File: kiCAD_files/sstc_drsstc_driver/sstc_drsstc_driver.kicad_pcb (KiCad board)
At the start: 2 copper layers, 90 x 90 mm, 80 parts, among them J1 Conn_01x02, J10 Conn_01x02, J11 Conn_01x03, J12 24V, J13 12V, J14 12V, J15 Conn_01x05, J16 Conn_01x05, J2 GDT, J3 Int_esp, J4 24V, J5 DRSSTC, J6 Conn_01x02, J7 SSTC, J8 DRSSTC, J9 SSTC_DUMMY, Q1 2N3904, U1 UCC27321P, U2 74HC14, U3 UCC27322P, U4 4N35, U5 ESP32-DEVKIT-V1, U7 74HC74, U8 LM7812_TO220, U9 LM7805_TO220

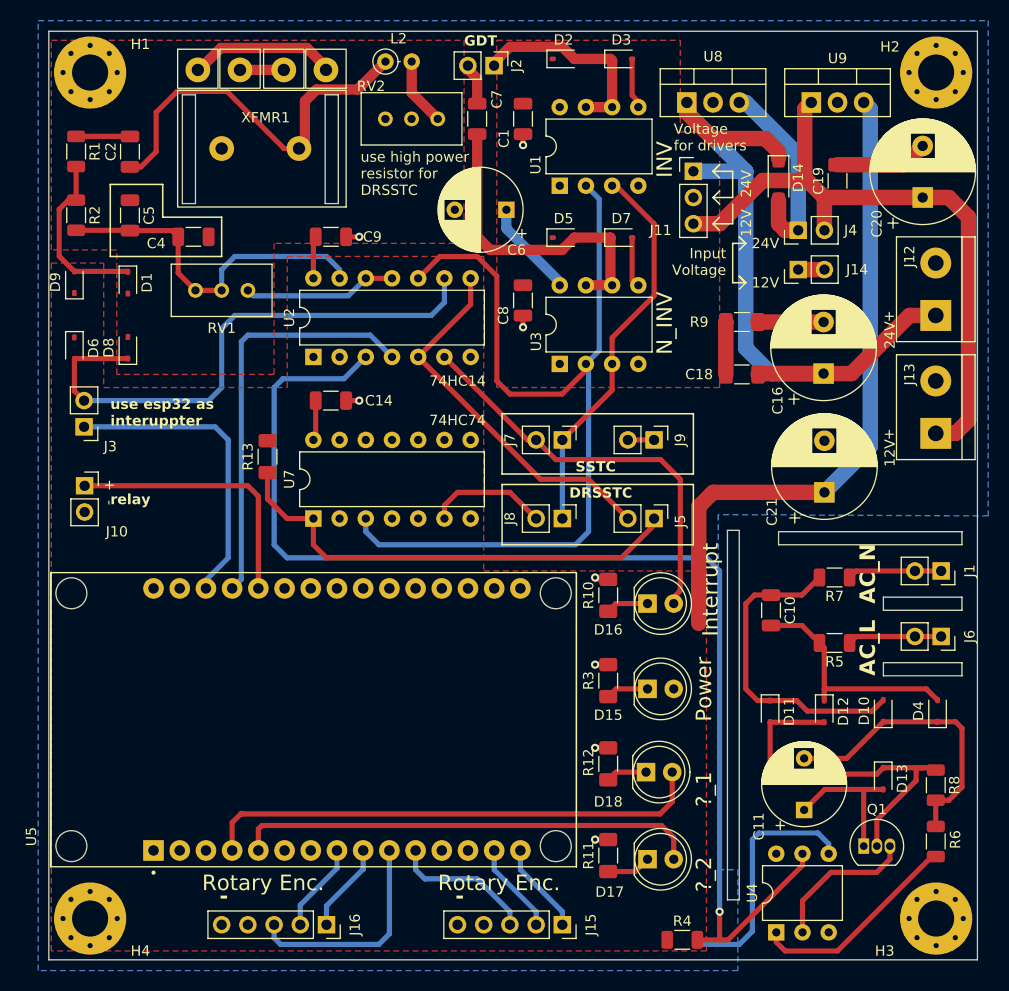
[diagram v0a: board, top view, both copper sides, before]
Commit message: Add files via upload
Rotary encoders are now connected to 3.3V instead of 5V
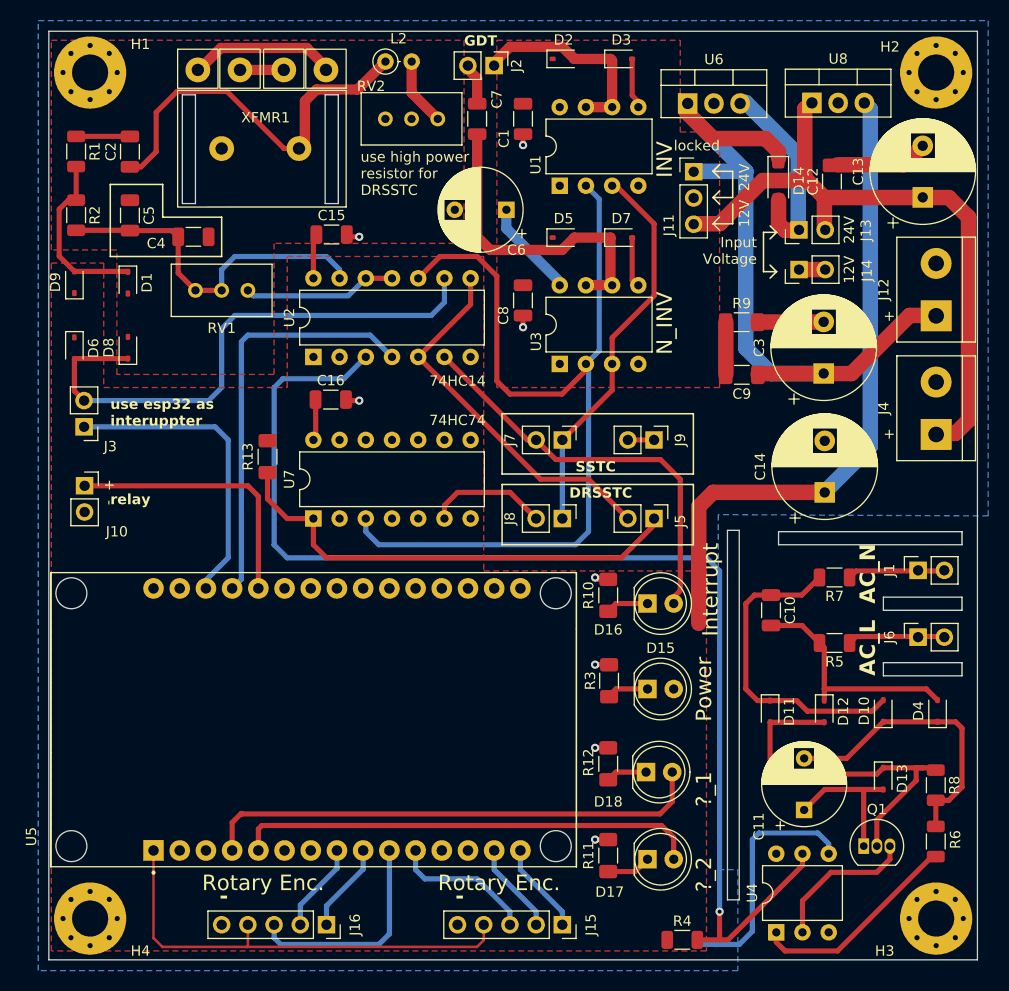
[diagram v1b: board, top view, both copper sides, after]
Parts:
- removed C18: 4.7u, Capacitor_SMD:C_1206_3216Metric_Pad1.33x1.80mm_HandSolder
- removed C19: 100n, Capacitor_SMD:C_1206_3216Metric_Pad1.33x1.80mm_HandSolder
- removed C20, C21: 330u, Capacitor_THT:CP_Radial_D10.0mm_P5.00mm
- removed U9: LM7805_TO220, Package_TO_SOT_THT:TO-220-3_Vertical
- added C12: 100n, Capacitor_SMD:C_1206_3216Metric_Pad1.33x1.80mm_HandSolder, F.Cu at (90.9, 29.6)
- added C13: 330u, Capacitor_THT:CP_Radial_D10.0mm_P5.00mm, F.Cu at (99.7, 31.1)
- added C15: 100n, Capacitor_SMD:C_1206_3216Metric, F.Cu at (42.4, 34.7)
- added C3: 330u, Capacitor_THT:CP_Radial_D10.0mm_P5.00mm, F.Cu at (90.1, 48.2)
- added U6: LM7812_TO220, Package_TO_SOT_THT:TO-220-3_Vertical, F.Cu at (76.9, 22.0)
- C14: value 100n -> 330u; footprint Capacitor_SMD:C_1206_3216Metric -> Capacitor_THT:CP_Radial_D10.0mm_P5.00mm
- C16: value 330u -> 100n; footprint Capacitor_THT:CP_Radial_D10.0mm_P5.00mm -> Capacitor_SMD:C_1206_3216Metric
- C9: value 100n -> 4.7u; footprint Capacitor_SMD:C_1206_3216Metric -> Capacitor_SMD:C_1206_3216Metric_Pad1.33x1.80mm_HandSolder
- J13: value 12V -> 24V; footprint TerminalBlock:TerminalBlock_bornier-2_P5.08mm -> Connector_PinHeader_2.54mm:PinHeader_1x02_P2.54mm_Vertical
- J4: value 24V -> 12V; footprint Connector_PinHeader_2.54mm:PinHeader_1x02_P2.54mm_Vertical -> TerminalBlock:TerminalBlock_bornier-2_P5.08mm
- U8: value LM7812_TO220 -> LM7805_TO220
- moved C14 48.7 mm to (90.2, 59.7), turned to 90 degrees
- moved C16 47.8 mm to (42.3, 50.7), turned to 0 degrees
- moved C9 42.0 mm to (82.2, 48.3), turned to 180 degrees
- moved J4 23.9 mm to (101.0, 54.1)
- moved J13 23.8 mm to (87.7, 34.2)
- moved U8 12.1 mm to (89.0, 21.9)
- moved J6 2.24 mm to (99.2, 73.7), turned to 90 degrees
- moved J1 2.24 mm to (99.2, 67.2), turned to 90 degrees
- moved D14 0.09 mm to (85.7, 29.5)
- moved R3 0.09 mm to (69.3, 78.0)
- moved J14 0.08 mm to (87.7, 38.1)
- moved J11 0.05 mm to (77.5, 28.6)
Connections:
- C16 pad 1: +24V -> +5V
- C9 pad 1: +5V -> +24V
- C9 pad 2: GND -> Net-(C9-Pad2)
- J13 pad 1: +12V -> Net-(D14-A)
- J13 pad 2: GND -> +12V
- J15 pad 4: +5V -> +3.3V
- J16 pad 4: +5V -> +3.3V
- J4 pad 1: Net-(D14-A) -> +12V
- J4 pad 2: +12V -> GND
- R9 pad 1: Net-(C18-Pad2) -> Net-(C9-Pad2)
- U5 pad 1: unconnected-(U5-3V3-Pad1) -> +3.3V
- U8 pad 1: +24V -> +12V
- U8 pad 3: Net-(D14-A) -> +5V
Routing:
- net +3.3V: track 0.00 -> 44.8 mm
- net Net-(C18-Pad2): track 5.09 -> 0.00 mm
- net Net-(C9-Pad2): track 0.00 -> 5.07 mm
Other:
- board text added: "locked"
- board text removed: "Voltage for drivers"
